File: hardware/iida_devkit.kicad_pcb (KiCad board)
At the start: 4 copper layers, 123.6 x 55.6 mm, 143 parts, among them J1 USB4085-GF-A, J10 Conn_01x04, J11 Conn_01x02, J12 Conn_01x06, J13 SIM_Card, J2 Batteries, J3 Conn_01x02, J4 Conn_01x02, J5 Conn_01x02, J6 TC2030, J7 Conn_01x06, J8 Conn_01x02, J9 Conn_01x06, Q1 PMOS, Q2 PMOS, Q3 PMOS, Q4 Q_NPN_BEC, U1 USBLC6-2SC6, U2 TLV76733DGNR, U3 AT25SF081B-SSHD-B, U4 MCP9808, U5 STM32L552CEU6, U6 SN74AVC4T245PW, U7 SARA-R500S-61B, Y1 ECS-160-9-37-CKM-TR3, Y2 ABS05-32.768KHZ-9-T

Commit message: HW: Update 0hm choice
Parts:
- R31: value ~ -> 0 Ω
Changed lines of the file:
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@@
 			)
 		)
-		(property "Value" "~"
+		(property "Value" "0 Ω"
 			(at -0.5 1.2 180)
 			(unlocked yes)
@@
 		(sheetname "Antenna")
 		(sheetfile "antenna.kicad_sch")
-		(attr smd exclude_from_bom dnp)
+		(attr smd)
 		(fp_line
 			(start 0.6 0.41)
@@
 			(layers "F.Cu" "F.Paste" "F.Mask")
 			(net 120 "/Antenna/ANT")
-			(pinfunction "Input")
-			(pintype "input")
+			(pintype "passive")
 		)
 		(pad "2" smd rect
@@
 			(layers "F.Cu" "F.Paste" "F.Mask")
 			(net 132 "/Antenna/ANT_EXT_SEL")
-			(pinfunction "A")
-			(pintype "output")
+			(pintype "passive")
 		)
 		(pad "3" smd rect
@@
 			(layers "F.Cu" "F.Paste" "F.Mask")
 			(net 133 "/Antenna/ANT_PCB_SEL")
-			(pinfunction "B")
-			(pintype "output")
+			(pintype "passive")
 		)
-		(model ":KICAD7_3DMODEL_DIR:Resistor_SMD.3dshapes/R_0402_1005Metric.step"
+		(model "${KICAD8_3DMODEL_DIR}/Resistor_SMD.3dshapes/R_0402_1005Metric.wrl"
 			(offset
-				(xyz 0.02 0 0)
+				(xyz -0.48 0 0)
 			)
 			(scale

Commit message: HW: Update BOM
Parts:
- D1, D2, D3: value Schottky -> CDBA140LL-HF
- J10: value Conn_01x04 -> PRPC004SAAN-RC
- J11, J3, J4, J5, J8: value Conn_01x02 -> PRPC001DAAN-RC
- J12, J7, J9: value Conn_01x06 -> PRPC006SAAN-RC
- J13: value SIM_Card -> SIM8070-6-0-11-00-A
- J2: value Batteries -> B2B-PH-K-S
- Q1, Q2, Q3: value PMOS -> FDN338P
- Q4: value Q_NPN_BEC -> MMBT3904-TP
- SW_SPST1: value RESET -> PTS645SK50SMTR92 LFS
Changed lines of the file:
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@@
 			)
 		)
+		(property "Digi-Key Part Number" "311-0.0JRCT-ND"
+			(at 0 0 180)
+			(unlocked yes)
+			(layer "F.Fab")
+			(hide yes)
+			(effects
+				(font
+					(size 1 1)
+					(thickness 0.15)
+				)
+			)
+		)
+		(property "Manufacturer" "YAGEO"
+			(at 0 0 180)
+			(unlocked yes)
+			(layer "F.Fab")
+			(hide yes)
+			(effects
+				(font
+					(size 1 1)
+					(thickness 0.15)
+				)
+			)
+		)
+		(property "Manufacturer Part Number" "RC0402JR-070RL"
+			(at 0 0 180)
+			(unlocked yes)
+			(layer "F.Fab")
+			(hide yes)
+			(effects
+				(font
+					(size 1 1)
+					(thickness 0.15)
+				)
+			)
+		)
 		(sheetname "Antenna")
 		(sheetfile "antenna.kicad_sch")
@@
 			)
 		)
-		(property "Value" "PMOS"
+		(property "Value" "FDN338P"
 			(at 0 2.4 0)
 			(layer "F.Fab")
@@
 			)
 		)
-		(property "Value" "Conn_01x06"
+		(property "Value" "PRPC006SAAN-RC"
 			(at 0 15.03 -90)
 			(layer "F.Fab")
@@
 			)
 		)
-		(property "Value" "Conn_01x04"
+		(property "Value" "PRPC004SAAN-RC"
 			(at 0 9.95 90)
 			(layer "F.Fab")
@@
 			)
 		)
-		(property "Value" "Q_NPN_BEC"
+		(property "Value" "MMBT3904-TP"
 			(at 0 2.4 90)
 			(layer "F.Fab")
@@
 			)
 		)
-		(property "Value" "PMOS"
+		(property "Value" "FDN338P"
 			(at 0 2.4 0)
 			(layer "F.Fab")
@@
 			)
 		)
-		(property "Value" "Schottky"
+		(property "Value" "CDBA140LL-HF"
 			(at 0 2.6 90)
 			(layer "F.Fab")
@@
 			)
 		)
-		(property "Value" "Batteries"
+		(property "Value" "B2B-PH-K-S"
 			(at 1 4 90)
 			(layer "F.Fab")
@@
 			)
 		)
-		(property "Value" "Schottky"
+		(property "Value" "CDBA140LL-HF"
 			(at 0 2.6 90)
 			(layer "F.Fab")
@@
 			)
 		)
+		(property "Digi-Key Part Number" "-"
+			(at 0 0 -90)
+			(unlocked yes)
+			(layer "F.Fab")
+			(hide yes)
+			(effects
+				(font
+					(size 1 1)
+					(thickness 0.15)
+				)
+			)
+		)
+		(property "Manufacturer" "-"
+			(at 0 0 -90)
+			(unlocked yes)
+			(layer "F.Fab")
+			(hide yes)
+			(effects
+				(font
+					(size 1 1)
+					(thickness 0.15)
+				)
+			)
+		)
+		(property "Manufacturer Part Number" "-"
+			(at 0 0 -90)
+			(unlocked yes)
+			(layer "F.Fab")
+			(hide yes)
+			(effects
+				(font
+					(size 1 1)
+					(thickness 0.15)
+				)
+			)
+		)
 		(sheetname "Antenna")
 		(sheetfile "antenna.kicad_sch")
@@
 			)
 		)
-		(property "Value" "Schottky"
+		(property "Value" "CDBA140LL-HF"
 			(at 0 2.6 90)
 			(layer "F.Fab")
@@
 			)
 		)
-		(property "Value" "Conn_01x06"
+		(property "Value" "PRPC006SAAN-RC"
 			(at 0 15.03 90)
 			(layer "F.Fab")
@@
 			)
 		)
-		(property "Value" "RESET"
+		(property "Value" "PTS645SK50SMTR92 LFS"
 			(at 0 4.15 0)
 			(layer "F.Fab")
@@
 			)
 		)
-		(property "Value" "Conn_01x02"
+		(property "Value" "PRPC001DAAN-RC"
 			(at 0 4.87 90)
 			(layer "F.Fab")
@@
 			)
 		)
-		(property "Value" "Conn_01x06"
+		(property "Value" "PRPC006SAAN-RC"
 			(at 0 15.03 360)
 			(layer "F.Fab")
@@
 			)
 		)
-		(property "Value" "PMOS"
+		(property "Value" "FDN338P"
 			(at 0 2.4 90)
 			(layer "F.Fab")
@@
 			)
 		)
-		(property "Value" "Conn_01x02"
+		(property "Value" "PRPC001DAAN-RC"
 			(at 0 4.87 0)
 			(layer "F.Fab")
@@
 			)
 		)
-		(property "Value" "Conn_01x02"
+		(property "Value" "PRPC001DAAN-RC"
 			(at 0 4.87 90)
 			(layer "F.Fab")
@@
 			)
 		)
-		(property "Value" "Conn_01x02"
+		(property "Value" "PRPC001DAAN-RC"
 			(at 0 4.87 90)
 			(layer "F.Fab")
@@
 			)
 		)
-		(property "Value" "SIM_Card"
+		(property "Value" "SIM8070-6-0-11-00-A"
 			(at 0 1 90)
 			(unlocked yes)
@@
 			)
 		)
-		(property "Value" "Conn_01x02"
+		(property "Value" "PRPC001DAAN-RC"
 			(at 0 4.87 0)
 			(layer "F.Fab")
@@
 	)
 	(zone
-		(net 125)
-		(net_name "/Antenna/ANT_PCB")
-		(layer "F.Cu")
-		(name "$teardrop_padvia$")
-		(hatch full 0.1)
-		(priority 30000)
-		(attr
-			(teardrop
-				(type padvia)
-			)
-		)
-		(connect_pads yes
-			(clearance 0)
-		)
-		(min_thickness 0.0254)
-		(filled_areas_thickness no)
-		(fill yes
-			(thermal_gap 0.5)
-			(thermal_bridge_width 0.5)
-			(island_removal_mode 1)
-			(island_area_min 10)
-		)
-		(polygon
-			(pts
-				(xy 196.45 77.9275) (xy 196.45 78.1725) (xy 196.95 78.3) (xy 197.201 78.05) (xy 196.95 77.8)
-			)
-		)
-	)
-	(zone
 		(net 1)
 		(net_name "GND")
@@
 			)
 		)
+	)
+	(zone
+		(net 125)
+		(net_name "/Antenna/ANT_PCB")
+		(layer "F.Cu")
+		(name "$teardrop_padvia$")
+		(hatch full 0.1)
+		(priority 30000)
+		(attr
+			(teardrop
+				(type padvia)
+			)
+		)
+		(connect_pads yes
+			(clearance 0)
+		)
+		(min_thickness 0.0254)
+		(filled_areas_thickness no)
+		(fill yes
+			(thermal_gap 0.5)
+			(thermal_bridge_width 0.5)
+			(island_removal_mode 1)
+			(island_area_min 10)
+		)
+		(polygon
+			(pts
+				(xy 196.45 77.9275) (xy 196.45 78.1725) (xy 196.95 78.3) (xy 197.201 78.05) (xy 196.95 77.8)
+			)
+		)

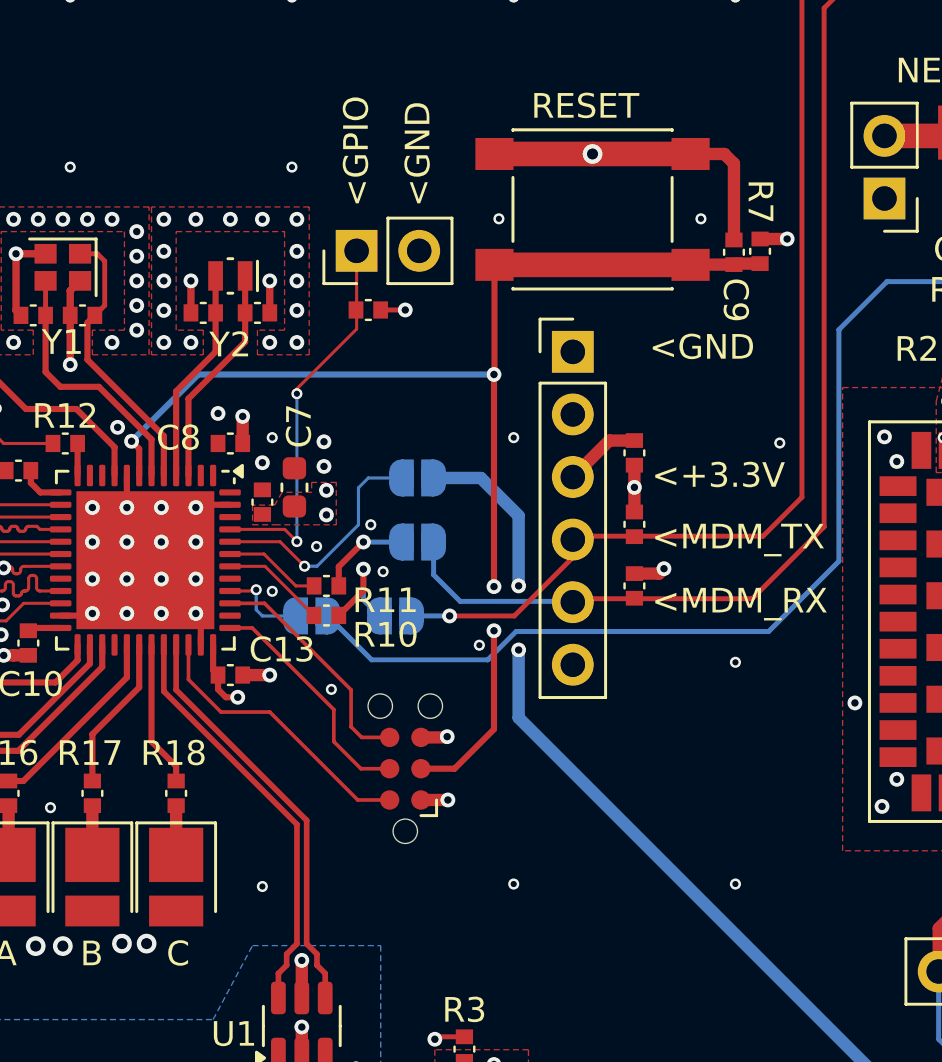
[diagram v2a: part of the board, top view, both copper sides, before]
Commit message: HW: TC2030 -> TC2050
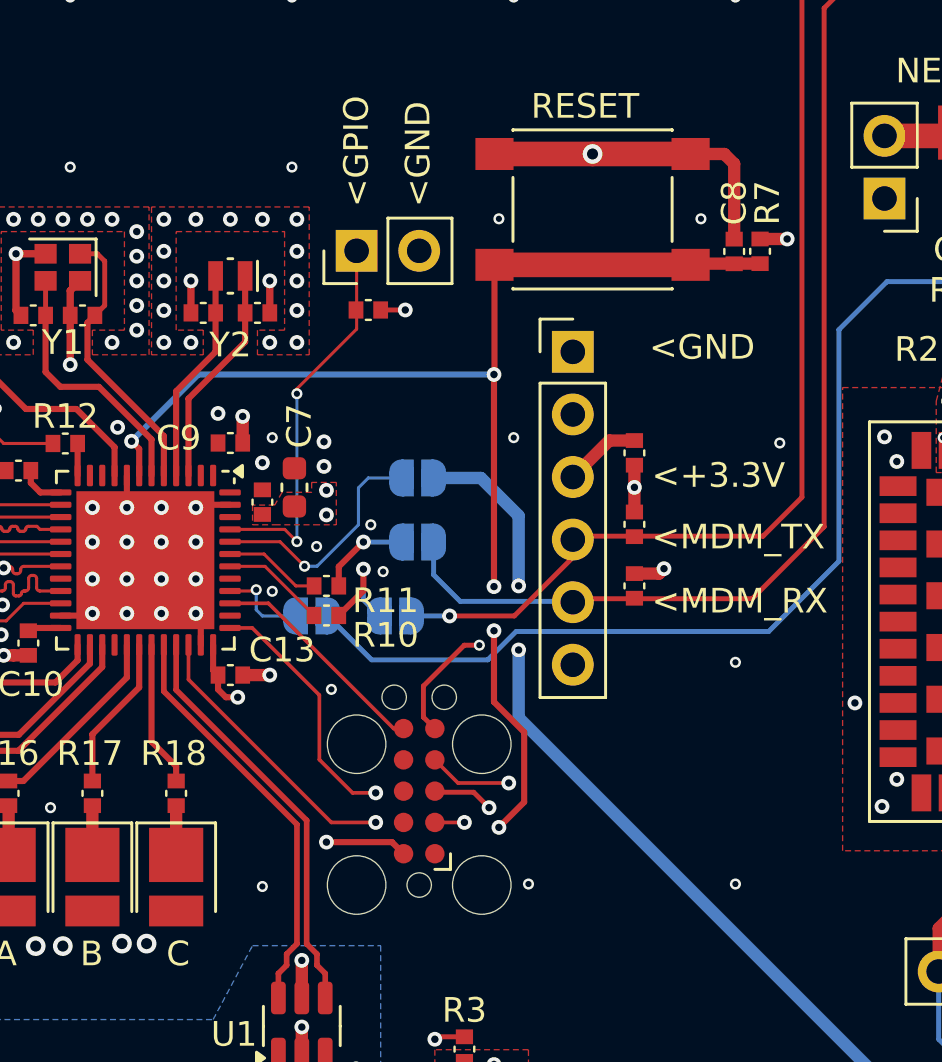
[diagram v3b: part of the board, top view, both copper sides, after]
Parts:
- J6: value TC2030 -> TC2050; footprint Connector:Tag-Connect_TC2030-IDC-NL_2x03_P1.27mm_Vertical -> Connector:Tag-Connect_TC2050-IDC-FP_2x05_P1.27mm_Vertical
- moved C8 21.9 mm to (152.9, 86.8), turned to -90 degrees
- moved C9 21.9 mm to (132.5, 94.6), turned to 0 degrees
- moved J6 1.07 mm to (140.2, 108.7)
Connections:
- C8 pad 1: /MCU/+3.3V -> GND
- C8 pad 2: GND -> /MCU/NRST
- C9 pad 1: GND -> /MCU/+3.3V
- C9 pad 2: /MCU/NRST -> GND
- J6 pad 3: /MCU/NRST -> GND
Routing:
- net /MCU/NRST: track 50.6 -> 62.5 mm, vias 4 -> 6
- net /MCU/SWCLK: track 9.61 -> 19.2 mm, vias 0 -> 2
- net GND: track 84.2 -> 90.4 mm
- net /MCU/SWDIO: track 11.6 -> 16.2 mm, vias 0 -> 2
- net /MCU/+3.3V: track 28.4 -> 27.3 mm, vias 21 -> 20

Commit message: HW: BOM consolidate
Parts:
- R22: value 1 kΩ -> 2.2 kΩ
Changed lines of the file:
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@@
 		)
 		(property "Footprint" "perfect_footprints:0402_1005_perfect"
-			(at 0 0 360)
+			(at 0 0 0)
 			(layer "F.Fab")
 			(hide yes)
@@
 		)
 		(property "Datasheet" ""
-			(at 0 0 360)
+			(at 0 0 0)
 			(layer "F.Fab")
 			(hide yes)
@@
 		)
 		(property "Description" ""
-			(at 0 0 360)
+			(at 0 0 0)
 			(layer "F.Fab")
 			(hide yes)
@@
 		)
 		(property "Footprint" "perfect_footprints:0402_1005_perfect"
-			(at 0 0 360)
+			(at 0 0 0)
 			(layer "F.Fab")
 			(hide yes)
@@
 		)
 		(property "Datasheet" ""
-			(at 0 0 360)
+			(at 0 0 0)
 			(layer "F.Fab")
 			(hide yes)
@@
 		)
 		(property "Description" ""
-			(at 0 0 360)
+			(at 0 0 0)
 			(layer "F.Fab")
 			(hide yes)
@@
 		)
 		(fp_text user "${REFERENCE}"
-			(at 0 3.81 360)
+			(at 0 3.81 0)
 			(layer "F.Fab")
 			(effects
@@
 		)
 		(property "Footprint" "perfect_footprints:0402_1005_perfect"
-			(at 0 0 360)
+			(at 0 0 0)
 			(layer "F.Fab")
 			(hide yes)
@@
 		)
 		(property "Datasheet" ""
-			(at 0 0 360)
+			(at 0 0 0)
 			(layer "F.Fab")
 			(hide yes)
@@
 		)
 		(property "Description" ""
-			(at 0 0 360)
+			(at 0 0 0)
 			(layer "F.Fab")
 			(hide yes)
@@
 			)
 		)
-		(property "Value" "1 kΩ"
+		(property "Value" "2.2 kΩ"
 			(at 0 1.2 -90)
 			(unlocked yes)
@@
 			)
 		)
-		(property "Manufacturer Part Number" "RC0402FR-071KL"
+		(property "Manufacturer Part Number" "RC0402FR-072K2L"
 			(at 0 0 -90)
 			(unlocked yes)
@@
 			)
 		)
-		(property "Digi-Key Part Number" "311-1.00KLRCT-ND"
+		(property "Digi-Key Part Number" "311-2.20KLRCT-ND"
 			(at 0 0 -90)
 			(unlocked yes)
@@
 		)
 		(property "Footprint" "perfect_footprints:0402_1005_perfect"
-			(at 0 0 360)
+			(at 0 0 0)
 			(layer "F.Fab")
 			(hide yes)
@@
 		)
 		(property "Datasheet" ""
-			(at 0 0 360)
+			(at 0 0 0)
 			(layer "F.Fab")
 			(hide yes)
@@
 		)
 		(property "Description" ""
-			(at 0 0 360)
+			(at 0 0 0)
 			(layer "F.Fab")
 			(hide yes)
@@
 		(tags "Through hole pin header THT 1x06 2.54mm single row")
 		(property "Reference" "J9"
-			(at 0 -2.33 360)
+			(at 0 -2.33 0)
 			(layer "F.SilkS")
 			(hide yes)
@@
 		)
 		(property "Value" "PRPC006SAAN-RC"
-			(at 0 15.03 360)
+			(at 0 15.03 0)
 			(layer "F.Fab")
 			(effects
@@
 		)
 		(property "Footprint" "perfect_footprints:0402_1005_perfect"
-			(at 0 0 360)
+			(at 0 0 0)
 			(layer "F.Fab")
 			(hide yes)
@@
 		)
 		(property "Datasheet" ""
-			(at 0 0 360)
+			(at 0 0 0)
 			(layer "F.Fab")
 			(hide yes)
@@
 		)
 		(property "Description" ""
-			(at 0 0 360)
+			(at 0 0 0)
 			(layer "F.Fab")
 			(hide yes)
@@
 		)
 		(fp_text user "${REFERENCE}"
-			(at 0 1.27 360)
+			(at 0 1.27 0)
 			(layer "F.Fab")
 			(effects
@@
 	)
 	(zone
-		(net 125)
-		(net_name "/Antenna/ANT_PCB")
-		(layer "F.Cu")
-		(name "$teardrop_padvia$")
-		(hatch full 0.1)
-		(priority 30000)
-		(attr
-			(teardrop
-				(type padvia)
-			)
-		)
-		(connect_pads yes
-			(clearance 0)
-		)
-		(min_thickness 0.0254)
-		(filled_areas_thickness no)
-		(fill yes
-			(thermal_gap 0.5)
-			(thermal_bridge_width 0.5)
-			(island_removal_mode 1)
-			(island_area_min 10)
-		)
-		(polygon
-			(pts
-				(xy 196.45 77.9275) (xy 196.45 78.1725) (xy 196.95 78.3) (xy 197.201 78.05) (xy 196.95 77.8)
-			)
-		)
-	)
-	(zone
 		(net 1)
 		(net_name "GND")
@@
 			)
 		)
+	)
+	(zone
+		(net 125)
+		(net_name "/Antenna/ANT_PCB")
+		(layer "F.Cu")
+		(name "$teardrop_padvia$")
+		(hatch full 0.1)
+		(priority 30000)
+		(attr
+			(teardrop
+				(type padvia)
+			)
+		)
+		(connect_pads yes
+			(clearance 0)
+		)
+		(min_thickness 0.0254)
+		(filled_areas_thickness no)
+		(fill yes
+			(thermal_gap 0.5)
+			(thermal_bridge_width 0.5)
+			(island_removal_mode 1)
+			(island_area_min 10)
+		)
+		(polygon
+			(pts
+				(xy 196.45 77.9275) (xy 196.45 78.1725) (xy 196.95 78.3) (xy 197.201 78.05) (xy 196.95 77.8)
+			)
+		)

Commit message: HW: Replace chinese NPN BJT
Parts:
- Q4: value MMBT3904-TP -> MMBT3904
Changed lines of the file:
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@@
 			)
 		)
-		(property "Value" "MMBT3904-TP"
+		(property "Value" "MMBT3904"
 			(at 0 2.4 90)
 			(layer "F.Fab")
@@
 			)
 		)
-		(property "Digi-Key Part Number" "MMBT3904TPMSCT-ND"
+		(property "Digi-Key Part Number" "4878-MMBT3904CT-ND"
 			(at 0 0 90)
 			(unlocked yes)
@@
 			)
 		)
-		(property "Manufacturer" "Micro Commercial Co"
+		(property "Manufacturer" "Diotec Semiconductor"
 			(at 0 0 90)
 			(unlocked yes)
@@
 			)
 		)
-		(property "Manufacturer Part Number" "MMBT3904-TP"
+		(property "Manufacturer Part Number" "MMBT3904"
 			(at 0 0 90)
 			(unlocked yes)
@@
 	)
 	(zone
-		(net 125)
-		(net_name "/Antenna/ANT_PCB")
-		(layer "F.Cu")
-		(name "$teardrop_padvia$")
-		(hatch full 0.1)
-		(priority 30000)
-		(attr
-			(teardrop
-				(type padvia)
-			)
-		)
-		(connect_pads yes
-			(clearance 0)
-		)
-		(min_thickness 0.0254)
-		(filled_areas_thickness no)
-		(fill yes
-			(thermal_gap 0.5)
-			(thermal_bridge_width 0.5)
-			(island_removal_mode 1)
-			(island_area_min 10)
-		)
-		(polygon
-			(pts
-				(xy 196.45 77.9275) (xy 196.45 78.1725) (xy 196.95 78.3) (xy 197.201 78.05) (xy 196.95 77.8)
-			)
-		)
-	)
-	(zone
 		(net 18)
 		(net_name "Net-(D2-A)")
@@
 			)
 		)
+	)
+	(zone
+		(net 125)
+		(net_name "/Antenna/ANT_PCB")
+		(layer "F.Cu")
+		(name "$teardrop_padvia$")
+		(hatch full 0.1)
+		(priority 30000)
+		(attr
+			(teardrop
+				(type padvia)
+			)
+		)
+		(connect_pads yes
+			(clearance 0)
+		)
+		(min_thickness 0.0254)
+		(filled_areas_thickness no)
+		(fill yes
+			(thermal_gap 0.5)
+			(thermal_bridge_width 0.5)
+			(island_removal_mode 1)
+			(island_area_min 10)
+		)
+		(polygon
+			(pts
+				(xy 196.45 77.9275) (xy 196.45 78.1725) (xy 196.95 78.3) (xy 197.201 78.05) (xy 196.95 77.8)
+			)
+		)

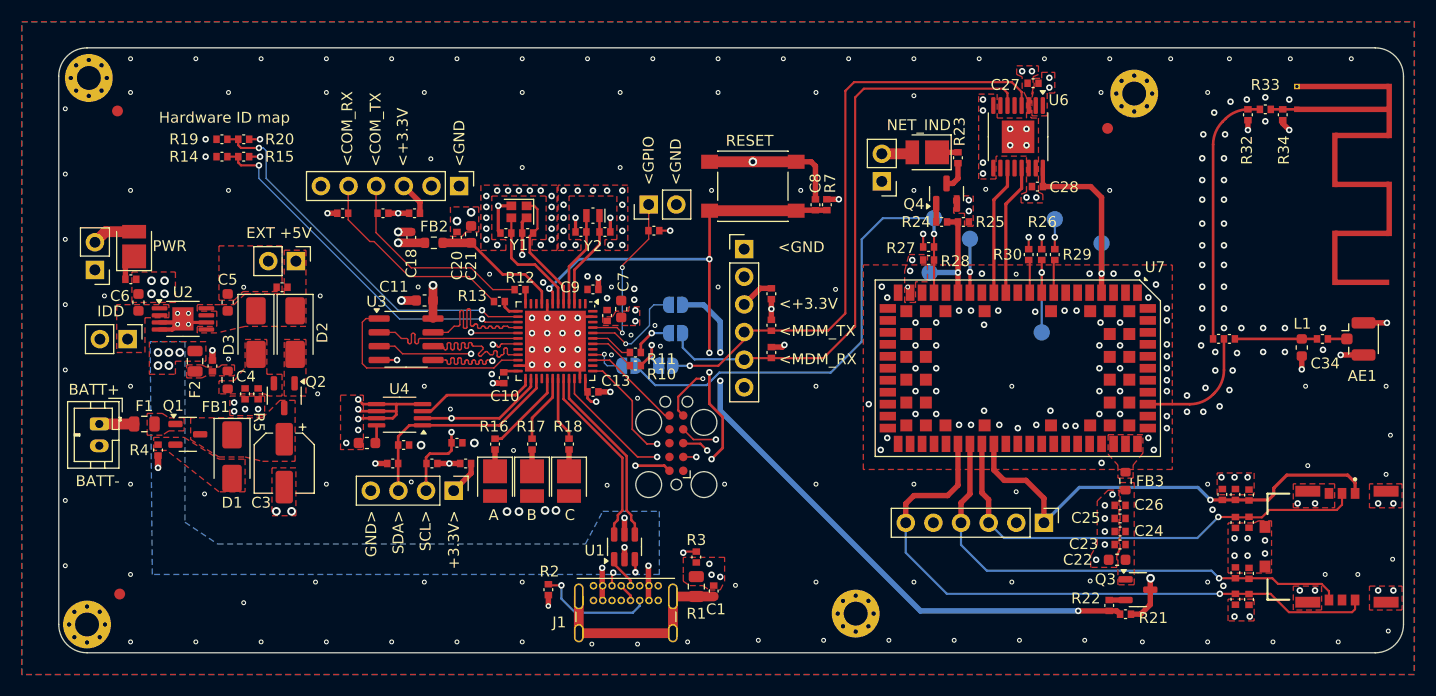
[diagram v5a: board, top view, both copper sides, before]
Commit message: HW: Connect +BATT to MCU
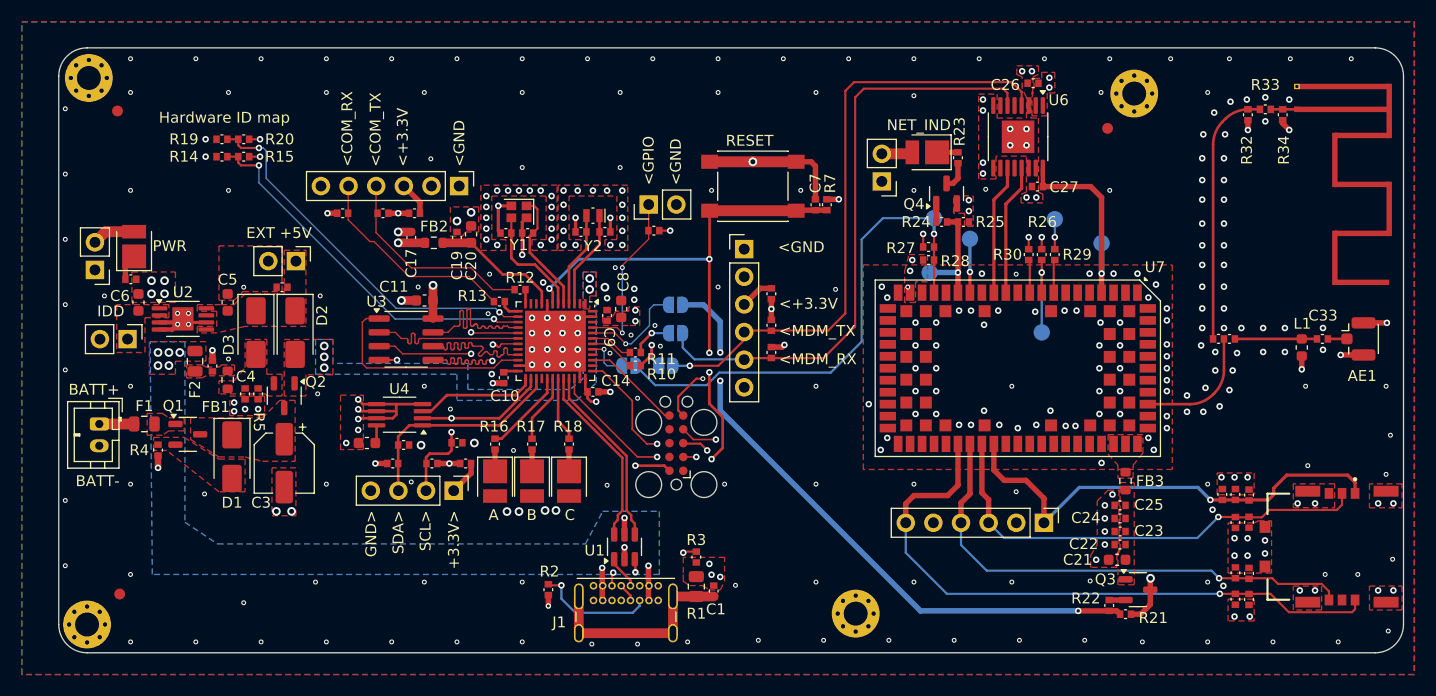
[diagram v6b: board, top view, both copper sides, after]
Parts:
- removed the C15 at (133.8, 97.0)
- moved C9 2.73 mm to (133.8, 97.0), turned to -90 degrees
- renumbered C14 to C13, C13 to C14, C16 to C15, C17 to C16, C18 to C17, C19 to C18, C20 to C19, C21 to C20, C22 to C21, C23 to C22, C24 to C23, C25 to C24, C26 to C25, C27 to C26, C28 to C27, C29 to C28, C30 to C29, C31 to C30, C32 to C31, C33 to C32, C34 to C33, C8 to C7, C7 to C8
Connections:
- net USB_DN renamed /MCU/USB_DN
- net USB_DP renamed /MCU/USB_DP
- D2 pad 2: Net-(D2-A) -> /MCU/+BATT
- Q2 pad 1: Net-(D2-A) -> /MCU/+BATT
- U5 pad 1: /MCU/+3.3V -> /MCU/+BATT
- U5 pad 40: Net-(JP4-A) -> unconnected-(U5-PB4-Pad40)
- U5 pad 41: unconnected-(U5-PB5-Pad41) -> Net-(JP4-A)
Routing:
- net GND: track 90.4 -> 89.3 mm, vias 376 -> 377
- net /MCU/+BATT: vias 0 -> 5
- net /MCU/+3.3V: vias 20 -> 19
- added copper zone on B.Cu, net /MCU/+BATT
- added copper zone on F.Cu, net /MCU/+BATT
- removed copper zone on F.Cu, net Net-(D2-A)
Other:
- board text added: "Iida devkit v4.2.0"
- board text removed: "Iida devkit v4.1.0"
